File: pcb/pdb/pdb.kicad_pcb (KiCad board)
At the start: 2 copper layers, 91 x 20 mm, 4 parts, among them J1 Conn_01x02, J2 Conn_01x02, J3 Conn_01x02, J4 Conn_01x02

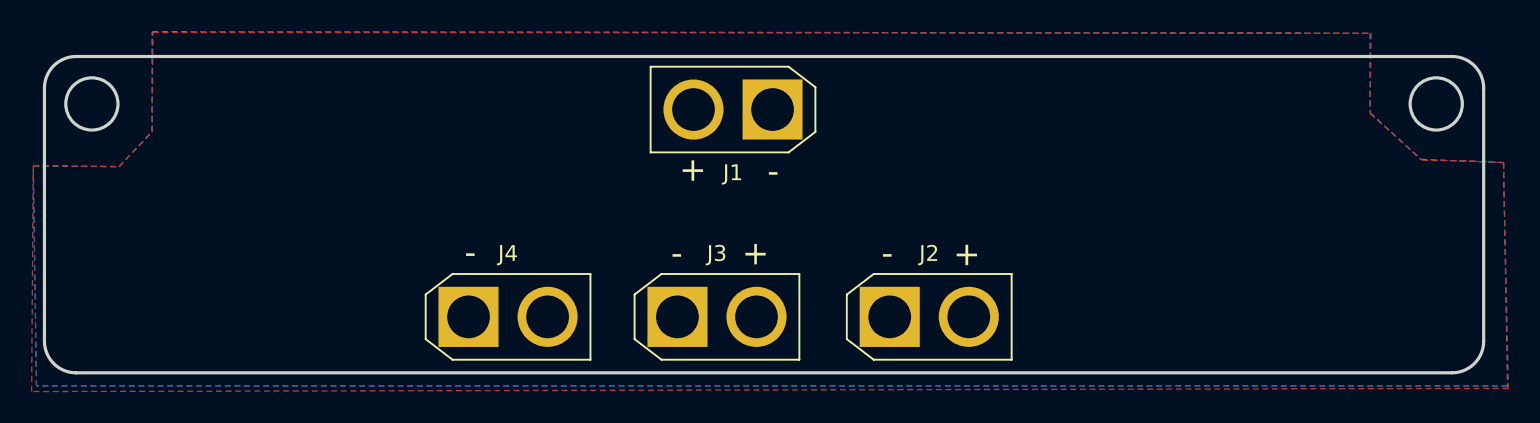
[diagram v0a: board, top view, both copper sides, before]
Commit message: feat: finish adding a connector
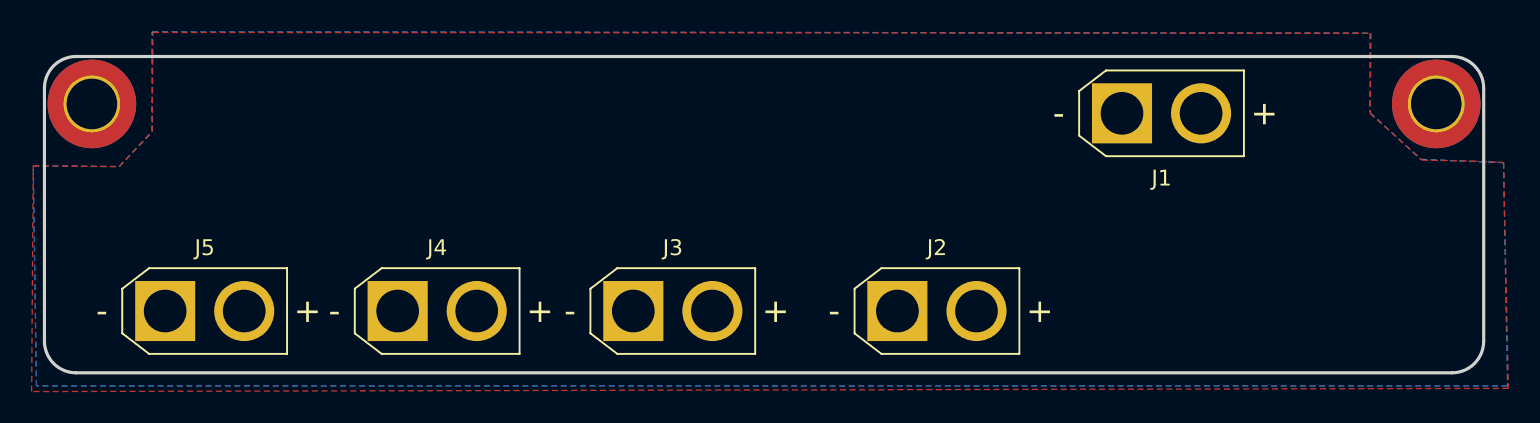
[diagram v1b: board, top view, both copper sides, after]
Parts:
- added H1: MountingHole, MountingHole:MountingHole_3.2mm_M3_Pad_TopBottom, F.Cu at (90.1, 89.3)
- added H2: MountingHole, MountingHole:MountingHole_3.2mm_M3_Pad_TopBottom, F.Cu at (175.1, 89.3)
- added J5: Conn_01x02, Connector_AMASS:AMASS_XT30U-M_1x02_P5.0mm_Vertical, F.Cu at (94.7, 102.4)
- moved J1 22.1 mm to (155.2, 89.9), turned to 0 degrees
- moved J4 4.50 mm to (109.4, 102.4)
- moved J3 2.82 mm to (124.3, 102.4)
- moved J2 0.61 mm to (141.0, 102.4)
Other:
- outline, holes or cut-outs redrawn

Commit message: feat: add DC jack & change XT30 footprint
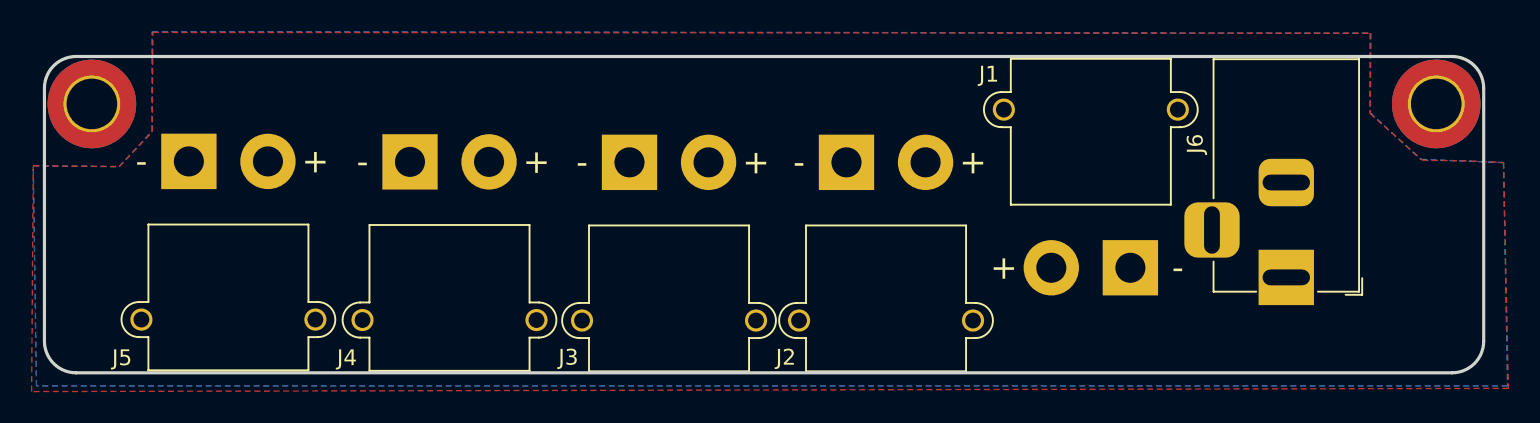
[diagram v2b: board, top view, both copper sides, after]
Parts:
- added J6: Jack-DC, Connector_BarrelJack:BarrelJack_Horizontal, F.Cu at (165.6, 100.3)
- J1, J2, J3, J4, J5: footprint Connector_AMASS:AMASS_XT30U-M_1x02_P5.0mm_Vertical -> Connector_AMASS:AMASS_XT30PW-M_1x02_P2.50mm_Horizontal
- moved J2 9.94 mm to (137.8, 93.0), turned to 180 degrees
- moved J1 9.78 mm to (155.7, 99.7)
- moved J5 9.58 mm to (96.2, 92.9), turned to 180 degrees
- moved J4 9.46 mm to (110.2, 93.0), turned to 180 degrees
- moved J3 9.40 mm to (124.1, 93.0), turned to 180 degrees
